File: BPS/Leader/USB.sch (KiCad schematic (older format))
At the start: 8 parts, among them J11 USB_B_Micro, U13 CP2102N-A01-GQFN24

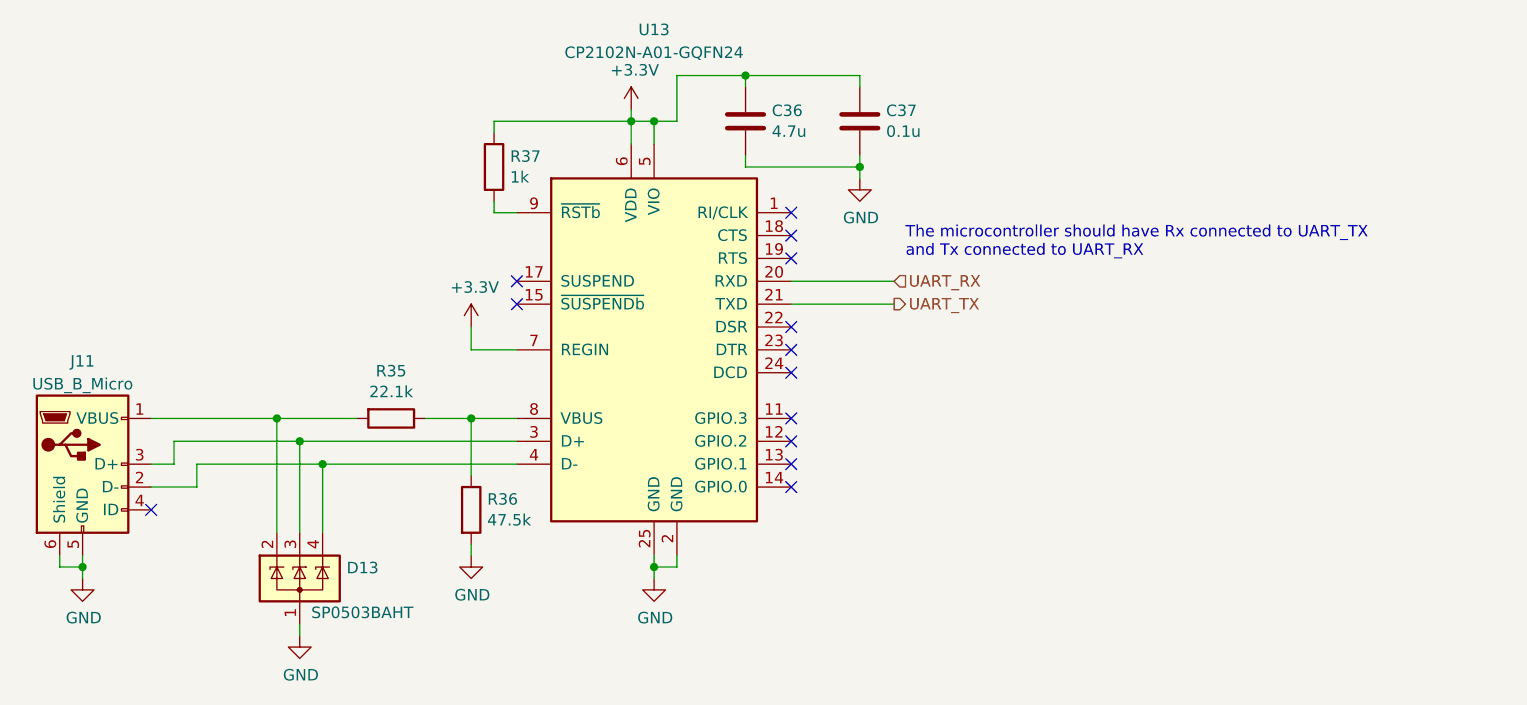
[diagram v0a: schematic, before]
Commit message: Places most components of leader board in their respective locations with nothing traced
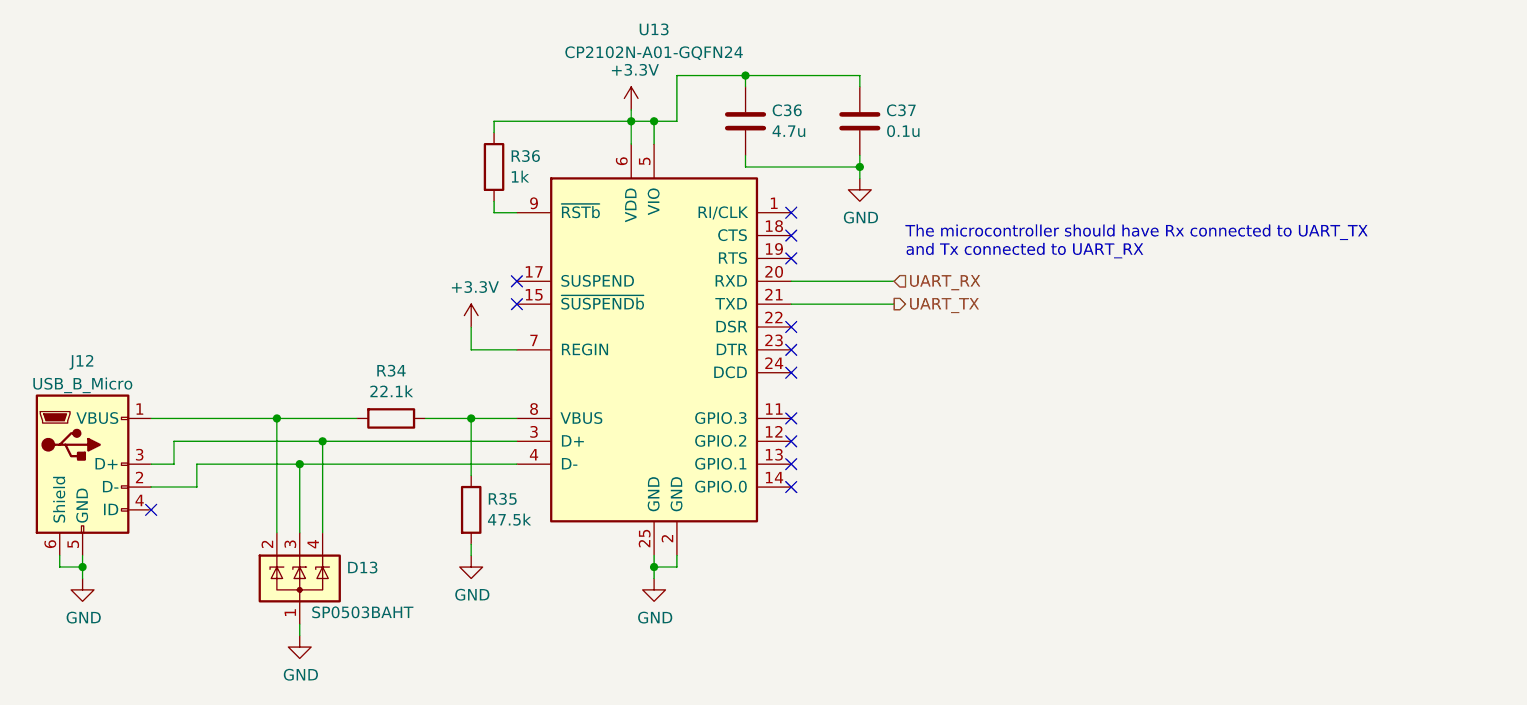
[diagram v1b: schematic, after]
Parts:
- renumbered J11 to J12, R35 to R34, R36 to R35, R37 to R36
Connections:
- net at J12.3 (D+), U13.3 (D+): now also D13.4 (K); no longer D13.3 (K)
- net at J12.2 (D-), U13.4 (D-): now also D13.3 (K); no longer D13.4 (K)
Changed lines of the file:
@@
 $EndComp
 $Comp
-L Connector:USB_B_Micro J11
+L Connector:USB_B_Micro J12
 U 1 1 5C4964BB
 P 3000 4300
-F 0 "J11" H 3000 4750 50  0000 C CNN
+F 0 "J12" H 3000 4750 50  0000 C CNN
 F 1 "USB_B_Micro" H 3000 4650 50  0000 C CNN
 F 2 "Connector_USB:USB_Micro-B_Molex-105017-0001" H 3150 4250 50  0001 C CNN
@@
 	3850 4600 3850 4100
 $Comp
-L Device:R R36
+L Device:R R35
 U 1 1 5C497DB9
 P 4700 4500
-F 0 "R36" H 4770 4546 50  0000 L CNN
+F 0 "R35" H 4770 4546 50  0000 L CNN
 F 1 "47.5k" H 4770 4455 50  0000 L CNN
 F 2 "Resistor_SMD:R_0805_2012Metric" V 4630 4500 50  0001 C CNN
@@
 $EndComp
 $Comp
-L Device:R R35
+L Device:R R34
 U 1 1 5C497DDB
 P 4350 4100
-F 0 "R35" V 4143 4100 50  0000 C CNN
+F 0 "R34" V 4143 4100 50  0000 C CNN
 F 1 "22.1k" V 4234 4100 50  0000 C CNN
 F 2 "Resistor_SMD:R_0805_2012Metric" V 4280 4100 50  0001 C CNN
@@
 Connection ~ 5400 2800
 $Comp
-L Device:R R37
+L Device:R R36
 U 1 1 5C49B01B
 P 4800 3000
-F 0 "R37" H 4870 3046 50  0000 L CNN
+F 0 "R36" H 4870 3046 50  0000 L CNN
 F 1 "1k" H 4870 2955 50  0000 L CNN
 F 2 "Resistor_SMD:R_0805_2012Metric" V 4730 3000 50  0001 C CNN
@@
 	3300 4100 3850 4100
 Wire Wire Line
-	3400 4200 3950 4200
-Wire Wire Line
-	3500 4300 4050 4300
-Wire Wire Line
-	4050 4600 4050 4300
-Connection ~ 4050 4300
-Wire Wire Line
-	4050 4300 4900 4300
-Wire Wire Line
-	3950 4200 3950 4600
-Connection ~ 3950 4200
-Wire Wire Line
-	3950 4200 4900 4200
+	3400 4200 4050 4200
+Wire Wire Line
+	3500 4300 3950 4300
+Wire Wire Line
+	3950 4600 3950 4300
+Connection ~ 3950 4300
+Wire Wire Line
+	3950 4300 4900 4300
+Wire Wire Line
+	4050 4600 4050 4200
+Connection ~ 4050 4200
+Wire Wire Line
+	4050 4200 4900 4200
 $EndSCHEMATC

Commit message: Adds power planes
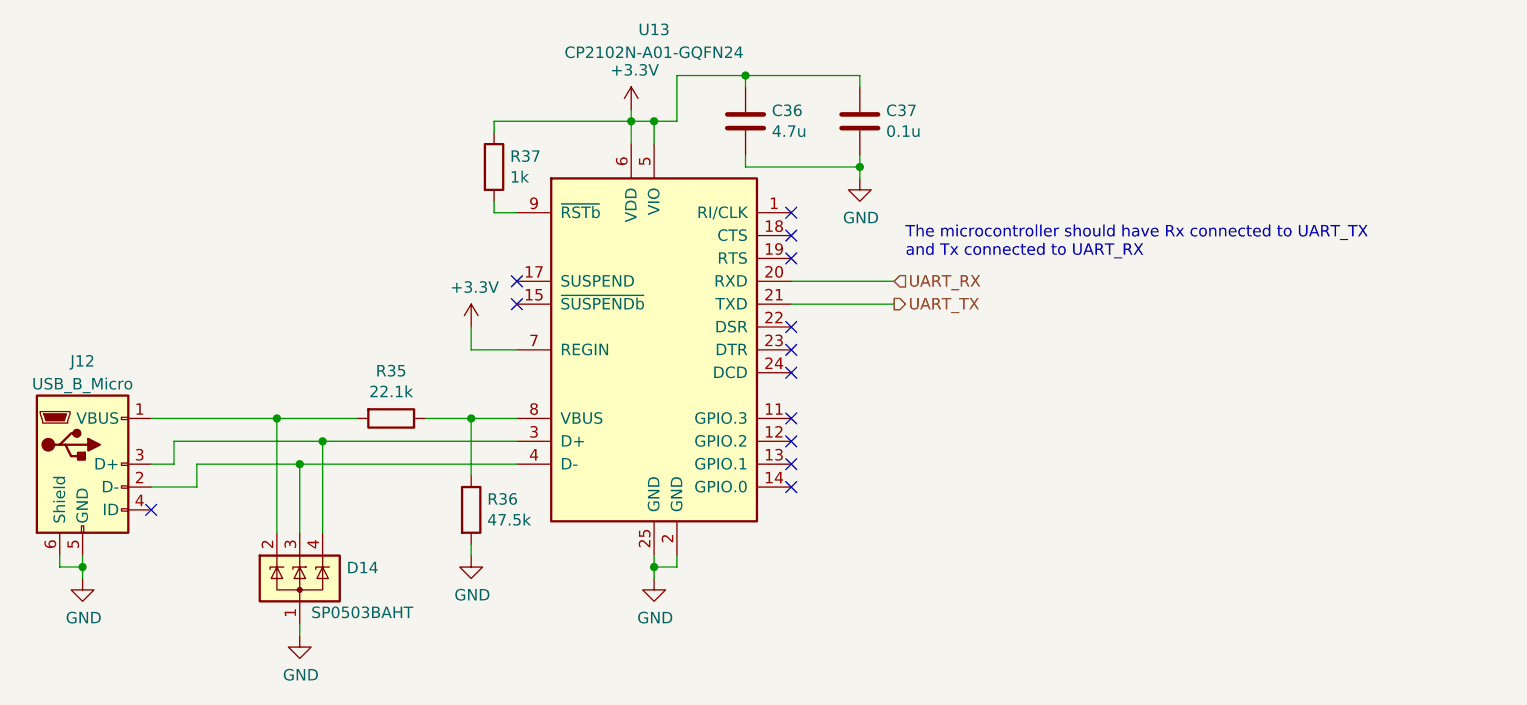
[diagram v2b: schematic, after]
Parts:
- renumbered D13 to D14, R34 to R35, R35 to R36, R36 to R37
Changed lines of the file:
@@
 	5500 4750 5500 4800
 $Comp
-L Power_Protection:SP0503BAHT D13
+L Power_Protection:SP0503BAHT D14
 U 1 1 5C496C9B
 P 3950 4800
-F 0 "D13" H 4155 4846 50  0000 L CNN
+F 0 "D14" H 4155 4846 50  0000 L CNN
 F 1 "SP0503BAHT" H 4000 4650 50  0000 L CNN
 F 2 "Package_TO_SOT_SMD:SOT-143" H 4175 4750 50  0001 L CNN
@@
 	3850 4600 3850 4100
 $Comp
-L Device:R R35
+L Device:R R36
 U 1 1 5C497DB9
 P 4700 4500
-F 0 "R35" H 4770 4546 50  0000 L CNN
+F 0 "R36" H 4770 4546 50  0000 L CNN
 F 1 "47.5k" H 4770 4455 50  0000 L CNN
 F 2 "Resistor_SMD:R_0805_2012Metric" V 4630 4500 50  0001 C CNN
@@
 $EndComp
 $Comp
-L Device:R R34
+L Device:R R35
 U 1 1 5C497DDB
 P 4350 4100
-F 0 "R34" V 4143 4100 50  0000 C CNN
+F 0 "R35" V 4143 4100 50  0000 C CNN
 F 1 "22.1k" V 4234 4100 50  0000 C CNN
 F 2 "Resistor_SMD:R_0805_2012Metric" V 4280 4100 50  0001 C CNN
@@
 Connection ~ 5400 2800
 $Comp
-L Device:R R36
+L Device:R R37
 U 1 1 5C49B01B
 P 4800 3000
-F 0 "R36" H 4870 3046 50  0000 L CNN
+F 0 "R37" H 4870 3046 50  0000 L CNN
 F 1 "1k" H 4870 2955 50  0000 L CNN
 F 2 "Resistor_SMD:R_0805_2012Metric" V 4730 3000 50  0001 C CNN

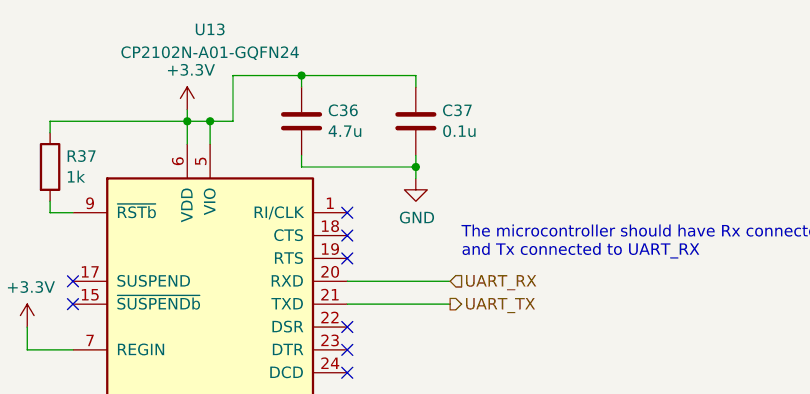
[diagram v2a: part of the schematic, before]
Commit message: Simplifies dc-dc converter schematics
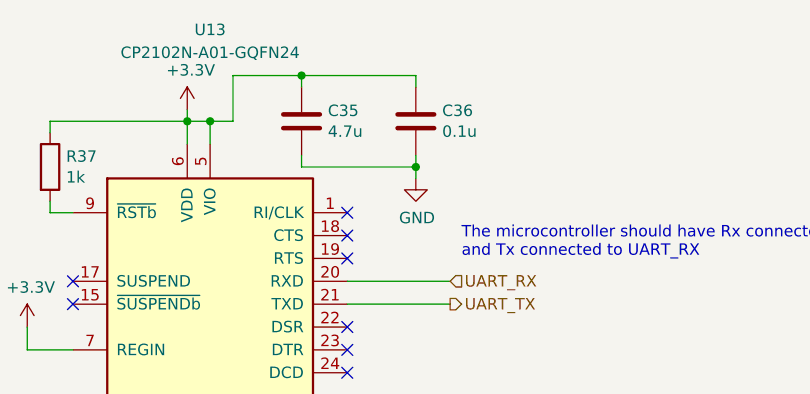
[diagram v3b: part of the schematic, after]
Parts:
- renumbered C36 to C35, C37 to C36
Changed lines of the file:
@@
 	3500 4400 3500 4300
 $Comp
-L power:GND #PWR074
+L power:GND #PWR073
 U 1 1 5C4965DF
 P 3000 4800
-F 0 "#PWR074" H 3000 4550 50  0001 C CNN
+F 0 "#PWR073" H 3000 4550 50  0001 C CNN
 F 1 "GND" H 3005 4627 50  0000 C CNN
 F 2 "" H 3000 4800 50  0001 C CNN
@@
 Connection ~ 3000 4750
 $Comp
-L power:GND #PWR079
+L power:GND #PWR078
 U 1 1 5C4966CF
 P 5500 4800
-F 0 "#PWR079" H 5500 4550 50  0001 C CNN
+F 0 "#PWR078" H 5500 4550 50  0001 C CNN
 F 1 "GND" H 5505 4627 50  0000 C CNN
 F 2 "" H 5500 4800 50  0001 C CNN
@@
 $EndComp
 $Comp
-L power:GND #PWR075
+L power:GND #PWR074
 U 1 1 5C497074
 P 3950 5050
-F 0 "#PWR075" H 3950 4800 50  0001 C CNN
+F 0 "#PWR074" H 3950 4800 50  0001 C CNN
 F 1 "GND" H 3955 4877 50  0000 C CNN
 F 2 "" H 3950 5050 50  0001 C CNN
@@
 	4200 4100 3850 4100
 $Comp
-L power:GND #PWR077
+L power:GND #PWR076
 U 1 1 5C498DBE
 P 4700 4700
-F 0 "#PWR077" H 4700 4450 50  0001 C CNN
+F 0 "#PWR076" H 4700 4450 50  0001 C CNN
 F 1 "GND" H 4705 4527 50  0000 C CNN
 F 2 "" H 4700 4700 50  0001 C CNN
@@
 	4700 4700 4700 4650
 $Comp
-L power:+3.3V #PWR078
+L power:+3.3V #PWR077
 U 1 1 5C499E7D
 P 5400 2750
-F 0 "#PWR078" H 5400 2600 50  0001 C CNN
+F 0 "#PWR077" H 5400 2600 50  0001 C CNN
 F 1 "+3.3V" H 5415 2923 50  0000 C CNN
 F 2 "" H 5400 2750 50  0001 C CNN
@@
 	4800 2800 5400 2800
 $Comp
-L Device:C C36
+L Device:C C35
 U 1 1 5C49CC52
 P 5900 2800
-F 0 "C36" H 6015 2846 50  0000 L CNN
+F 0 "C35" H 6015 2846 50  0000 L CNN
 F 1 "4.7u" H 6015 2755 50  0000 L CNN
 F 2 "Capacitor_SMD:C_0805_2012Metric" H 5938 2650 50  0001 C CNN
@@
 NoConn ~ 6100 4400
 $Comp
-L power:+3.3V #PWR076
+L power:+3.3V #PWR075
 U 1 1 5C4A2CBF
 P 4700 3700
-F 0 "#PWR076" H 4700 3550 50  0001 C CNN
+F 0 "#PWR075" H 4700 3550 50  0001 C CNN
 F 1 "+3.3V" H 4715 3873 50  0000 C CNN
 F 2 "" H 4700 3700 50  0001 C CNN
@@
 	4700 3800 4900 3800
 $Comp
-L Device:C C37
+L Device:C C36
 U 1 1 5C4A4791
 P 6400 2800
-F 0 "C37" H 6515 2846 50  0000 L CNN
+F 0 "C36" H 6515 2846 50  0000 L CNN
 F 1 "0.1u" H 6515 2755 50  0000 L CNN
 F 2 "Capacitor_SMD:C_0805_2012Metric" H 6438 2650 50  0001 C CNN
@@
 $EndComp
 $Comp
-L power:GND #PWR080
+L power:GND #PWR079
 U 1 1 5C4A4BE4
 P 6400 3050
-F 0 "#PWR080" H 6400 2800 50  0001 C CNN
+F 0 "#PWR079" H 6400 2800 50  0001 C CNN
 F 1 "GND" H 6405 2877 50  0000 C CNN
 F 2 "" H 6400 3050 50  0001 C CNN
